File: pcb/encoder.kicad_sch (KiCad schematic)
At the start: 5 parts, among them J17 Conn_01x04_Pin

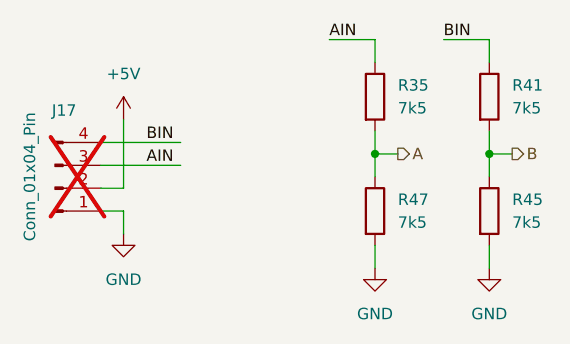
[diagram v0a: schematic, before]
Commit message: Fix encoder pull downs
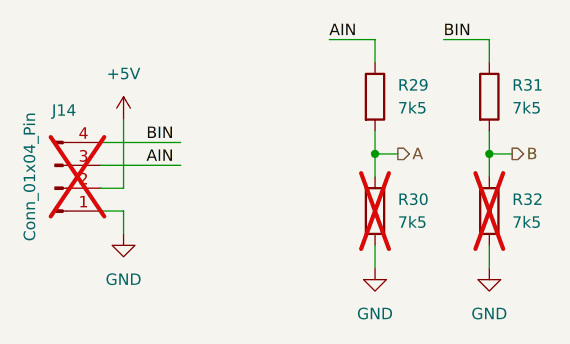
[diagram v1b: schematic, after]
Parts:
- R30: renamed from R47; now not fitted; now left out of the parts list
- R32: renamed from R45; now not fitted; now left out of the parts list
- renumbered J17 to J14, R35 to R29, R41 to R31
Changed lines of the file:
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@@
 (kicad_sch
-	(version 20231120)
+	(version 20250114)
 	(generator "eeschema")
-	(generator_version "8.0")
+	(generator_version "9.0")
 	(paper "A5")
 	(junction
@@
 	(label "AIN"
 		(at 86.36 41.91 0)
-		(fields_autoplaced yes)
 		(effects
 			(font
@@
 	(label "BIN"
 		(at 99.06 41.91 0)
-		(fields_autoplaced yes)
 		(effects
 			(font
@@
 	(label "AIN"
 		(at 66.04 55.88 0)
-		(fields_autoplaced yes)
 		(effects
 			(font
@@
 	(label "BIN"
 		(at 66.04 53.34 0)
-		(fields_autoplaced yes)
 		(effects
 			(font
@@
 		(shape output)
 		(at 93.98 54.61 0)
-		(fields_autoplaced yes)
 		(effects
 			(font
@@
 		(shape output)
 		(at 106.68 54.61 0)
-		(fields_autoplaced yes)
 		(effects
 			(font
@@
 		(dnp no)
 		(fields_autoplaced yes)
-		(property "Reference" "#PWR0187"
+		(property "Reference" "#PWR0109"
 			(at 63.5 54.61 0)
 			(effects
@@
 		(dnp no)
 		(fields_autoplaced yes)
-		(property "Reference" "#PWR0193"
+		(property "Reference" "#PWR0115"
 			(at 91.44 73.66 0)
 			(effects
@@
 		(dnp no)
 		(fields_autoplaced yes)
-		(property "Reference" "#PWR0196"
+		(property "Reference" "#PWR0118"
 			(at 104.14 73.66 0)
 			(effects
@@
 		(unit 1)
 		(exclude_from_sim no)
-		(in_bom yes)
+		(in_bom no)
 		(on_board yes)
-		(dnp no)
+		(dnp yes)
 		(fields_autoplaced yes)
-		(property "Reference" "R47"
+		(property "Reference" "R30"
 			(at 93.98 59.6899 0)
 			(effects
@@
 		(dnp no)
 		(fields_autoplaced yes)
-		(property "Reference" "#PWR0188"
+		(property "Reference" "#PWR0110"
 			(at 63.5 69.85 0)
 			(effects
@@
 		(unit 1)
 		(exclude_from_sim no)
-		(in_bom yes)
+		(in_bom no)
 		(on_board yes)
-		(dnp no)
+		(dnp yes)
 		(fields_autoplaced yes)
-		(property "Reference" "R45"
+		(property "Reference" "R32"
 			(at 106.68 59.6899 0)
 			(effects
@@
 		(dnp no)
 		(fields_autoplaced yes)
-		(property "Reference" "R41"
+		(property "Reference" "R31"
 			(at 106.68 46.9899 0)
 			(effects
@@
 		(dnp no)
 		(fields_autoplaced yes)
-		(property "Reference" "R35"
+		(property "Reference" "R29"
 			(at 93.98 46.9899 0)
 			(effects
@@
 		(on_board yes)
 		(dnp yes)
-		(property "Reference" "J17"
+		(property "Reference" "J14"
 			(at 56.896 49.784 0)
 			(effects
